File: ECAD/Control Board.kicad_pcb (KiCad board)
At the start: 2 copper layers, 266.1 x 97.2 mm, 77 parts, among them J3 Thermocouple, J4 SD_Card, J5 PWR/Heat, J6 FAN, J7 UPDI, Q1 IPD50N06S4L08, Q2 IPD50N06S4L08, SW1 Reflow, SW2 Stop, SW3 Set temp mode, U1 ATtiny1614-SS, U2 LD1086DT33, U3 AD8497, U4 HT16K33, U5 LM2575HVS-ADJ

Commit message: More routing
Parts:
- moved R5 28.9 mm to (162.8, 77.6)
- moved J7 28.9 mm to (168.9, 75.1)
- moved C12 13.7 mm to (75.8, 104.9)
- moved RV1 13.7 mm to (72.0, 101.1)
- moved R34 5.08 mm to (202.6, 47.0)
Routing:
- net /TempCtrl: track 108.9 -> 7.68 mm
- net /H-: track 0.00 -> 23.1 mm
- net GND: track 82.4 -> 104.7 mm
- net +3V3: track 174.7 -> 156.3 mm
- net Net-(Q1-Pad1): track 5.79 -> 9.46 mm
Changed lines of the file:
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@@
-(kicad_pcb (version 20171130) (host pcbnew "(5.1.9)-1")
+(kicad_pcb (version 20171130) (host pcbnew "(5.1.10)-1")
   (general
     (thickness 1.6)
     (drawings 27)
-    (tracks 444)
+    (tracks 448)
     (zones 0)
     (modules 77)
@@
   )
   (setup
-    (last_trace_width 2.032)
+    (last_trace_width 0.508)
     (user_trace_width 0.254)
     (user_trace_width 0.381)
@@
     (add_net /TOUT)
     (add_net /TempCtrl)
-    (add_net /WRPrt)
     (add_net GND)
     (add_net "Net-(C10-Pad1)")
@@
     (add_net "Net-(D5-Pad2)")
     (add_net "Net-(D6-Pad1)")
-    (add_net "Net-(DS1-Pad3)")
-    (add_net "Net-(DS2-Pad3)")
-    (add_net "Net-(DS3-Pad3)")
     (add_net "Net-(J3-Pad1)")
     (add_net "Net-(J3-Pad2)")
-    (add_net "Net-(J4-Pad8)")
-    (add_net "Net-(J4-Pad9)")
     (add_net "Net-(J7-Pad2)")
     (add_net "Net-(Q1-Pad1)")
@@
     (add_net "Net-(R30-Pad1)")
     (add_net "Net-(R31-Pad1)")
-    (add_net "Net-(U3-Pad4)")
-    (add_net "Net-(U4-Pad10)")
-    (add_net "Net-(U4-Pad11)")
-    (add_net "Net-(U4-Pad8)")
-    (add_net "Net-(U4-Pad9)")
     (add_net VCC)
   )
@@
   )
   (module Resistor_SMD:R_1206_3216Metric_Pad1.30x1.75mm_HandSolder (layer F.Cu)
-    (at 197.485 46.99 270)
+    (at 202.565 46.99 270)
     (descr "Resistor SMD 1206 (3216 Metric), square (rectangular) end terminal, IPC_7351 nominal with elongated pad for handsoldering. (Body size source: IPC-SM-782 page 72, https://www.pcb-3d.com/wordpress/wp-content/uploads/ipc-sm-782a_amendment_1_and_2.pdf), generated with kicad-footprint-generator")
     (tags "resistor handsolder")
@@
   )
   (module Connector_PinHeader_2.54mm:PinHeader_1x03_P2.54mm_Vertical (layer B.Cu)
-    (at 60.325 93.98 180)
+    (at 72.009 101.092 180)
     (descr "Through hole straight pin header, 1x03, 2.54mm pitch, single row")
     (tags "Through hole pin header THT 1x03 2.54mm single row")
@@
   )
   (module Resistor_SMD:R_1206_3216Metric_Pad1.30x1.75mm_HandSolder (layer F.Cu)
-    (at 167.92 106.045)
+    (at 162.84 77.597)
     (descr "Resistor SMD 1206 (3216 Metric), square (rectangular) end terminal, IPC_7351 nominal with elongated pad for handsoldering. (Body size source: IPC-SM-782 page 72, https://www.pcb-3d.com/wordpress/wp-content/uploads/ipc-sm-782a_amendment_1_and_2.pdf), generated with kicad-footprint-generator")
     (tags "resistor handsolder")
@@
   )
   (module Connector_PinHeader_2.54mm:PinHeader_1x03_P2.54mm_Vertical (layer B.Cu)
-    (at 173.99 103.505 180)
+    (at 168.91 75.057 180)
     (descr "Through hole straight pin header, 1x03, 2.54mm pitch, single row")
     (tags "Through hole pin header THT 1x03 2.54mm single row")
@@
   )
   (module Capacitor_SMD:C_0805_2012Metric_Pad1.18x1.45mm_HandSolder (layer F.Cu)
-    (at 64.135 97.79 270)
+    (at 75.819 104.902 270)
     (descr "Capacitor SMD 0805 (2012 Metric), square (rectangular) end terminal, IPC_7351 nominal with elongated pad for handsoldering. (Body size source: IPC-SM-782 page 76, https://www.pcb-3d.com/wordpress/wp-content/uploads/ipc-sm-782a_amendment_1_and_2.pdf, https://docs.google.com/spreadsheets/d/1BsfQQcO9C6DZCsRaXUlFlo91Tg2WpOkGARC1WS5S8t0/edit?usp=sharing), generated with kicad-footprint-generator")
     (tags "capacitor handsolder")
@@
     (effects (font (size 1 1) (thickness 0.15)) (justify mirror))
   )
-  (gr_text UPDI (at 173.99 111.125) (layer B.SilkS)
+  (gr_text UPDI (at 168.91 82.677) (layer B.SilkS)
     (effects (font (size 1 1) (thickness 0.15)) (justify mirror))
   )
@@
   (segment (start 61.305188 73.4275) (end 59.957688 72.08) (width 0.381) (layer F.Cu) (net 1))
   (segment (start 69.469 73.4275) (end 61.305188 73.4275) (width 0.381) (layer F.Cu) (net 1))
-  (segment (start 63.9025 99.06) (end 64.135 98.8275) (width 0.508) (layer F.Cu) (net 1))
-  (segment (start 60.325 99.06) (end 63.9025 99.06) (width 0.508) (layer F.Cu) (net 1))
+  (segment (start 75.5865 106.172) (end 75.819 105.9395) (width 0.508) (layer F.Cu) (net 1))
+  (segment (start 72.009 106.172) (end 75.5865 106.172) (width 0.508) (layer F.Cu) (net 1))
   (via (at 132.715 75.565) (size 1) (drill 0.5) (layers F.Cu B.Cu) (net 1))
   (via (at 146.05 59.055) (size 1) (drill 0.5) (layers F.Cu B.Cu) (net 1))
@@
   (via (at 120.65 92.71) (size 1) (drill 0.5) (layers F.Cu B.Cu) (net 1))
   (via (at 83.82 97.155) (size 1) (drill 0.5) (layers F.Cu B.Cu) (net 1))
-  (via (at 66.04 99.06) (size 1) (drill 0.5) (layers F.Cu B.Cu) (net 1))
+  (via (at 77.724 106.172) (size 1) (drill 0.5) (layers F.Cu B.Cu) (net 1))
   (via (at 61.214 56.515) (size 1) (drill 0.5) (layers F.Cu B.Cu) (net 1))
   (via (at 68.199 75.692) (size 1) (drill 0.5) (layers F.Cu B.Cu) (net 1))
@@
   (segment (start 218.05 101.6) (end 217.805 101.355) (width 2.032) (layer F.Cu) (net 1))
   (segment (start 227.965 101.6) (end 218.05 101.6) (width 2.032) (layer F.Cu) (net 1))
+  (via (at 212.725 95.25) (size 1) (drill 0.5) (layers F.Cu B.Cu) (net 1))
+  (segment (start 222.57 55.88) (end 232.41 65.72) (width 2.54) (layer F.Cu) (net 1))
+  (segment (start 214.19 55.88) (end 222.57 55.88) (width 2.54) (layer F.Cu) (net 1))
   (segment (start 66.8515 71.43) (end 66.929 71.3525) (width 0.381) (layer F.Cu) (net 2))
   (segment (start 63.3265 71.43) (end 66.8515 71.43) (width 0.381) (layer F.Cu) (net 2))
@@
   (segment (start 71.0985 71.3525) (end 69.469 71.3525) (width 0.508) (layer F.Cu) (net 2))
   (segment (start 83.184994 93.98) (end 84.328 92.836994) (width 0.508) (layer B.Cu) (net 2))
-  (segment (start 60.325 93.98) (end 83.184994 93.98) (width 0.508) (layer B.Cu) (net 2))
+  (segment (start 192.945 62.77) (end 193.04 62.865) (width 1.27) (layer F.Cu) (net 2))
+  (segment (start 192.945 58.42) (end 192.945 62.77) (width 1.27) (layer F.Cu) (net 2))
   (segment (start 232.41 84.78) (end 232.41 75.25) (width 2.54) (layer F.Cu) (net 3))
   (segment (start 208.175 92.955) (end 207.87 92.65) (width 1.27) (layer F.Cu) (net 3))
   (segment (start 217.805 92.955) (end 208.175 92.955) (width 1.27) (layer F.Cu) (net 3))
+  (segment (start 224.235 92.955) (end 232.41 84.78) (width 2.032) (layer F.Cu) (net 3))
+  (segment (start 217.805 92.955) (end 224.235 92.955) (width 2.032) (layer F.Cu) (net 3))
+  (segment (start 217.805 92.955) (end 217.805 87.63) (width 2.032) (layer F.Cu) (net 3))
   (segment (start 201.93 58.42) (end 194.945 58.42) (width 0.762) (layer F.Cu) (net 4))
   (segment (start 202.19 58.16) (end 201.93 58.42) (width 1.27) (layer F.Cu) (net 4))
@@
   (segment (start 63.754 64.06) (end 63.754 67.31) (width 0.381) (layer F.Cu) (net 6))
   (segment (start 62.019 67.31) (end 63.754 67.31) (width 0.381) (layer F.Cu) (net 6))
-  (segment (start 63.9025 96.52) (end 64.135 96.7525) (width 0.508) (layer F.Cu) (net 7))
-  (segment (start 60.325 96.52) (end 63.9025 96.52) (width 0.508) (layer F.Cu) (net 7))
-  (segment (start 65.589558 96.7525) (end 64.135 96.7525) (width 0.381) (layer F.Cu) (net 7))
-  (segment (start 71.199058 102.362) (end 65.589558 96.7525) (width 0.381) (layer F.Cu) (net 7))
-  (segment (start 163.068 102.362) (end 71.199058 102.362) (width 0.381) (layer F.Cu) (net 7))
+  (segment (start 75.5865 103.632) (end 75.819 103.8645) (width 0.508) (layer F.Cu) (net 7))
+  (segment (start 72.009 103.632) (end 75.5865 103.632) (width 0.508) (layer F.Cu) (net 7))
   (segment (start 165.735 99.695) (end 163.068 102.362) (width 0.381) (layer F.Cu) (net 7))
   (segment (start 176.175 77.995) (end 175.65 77.47) (width 0.508) (layer F.Cu) (net 8))
@@
   (segment (start 63.754 53.721) (end 66.675 50.8) (width 0.381) (layer F.Cu) (net 31))
   (segment (start 63.754 58.42) (end 63.754 53.721) (width 0.381) (layer F.Cu) (net 31))
-  (via (at 212.725 95.25) (size 1) (drill 0.5) (layers F.Cu B.Cu) (net 1))
-  (segment (start 224.235 92.955) (end 232.41 84.78) (width 2.032) (layer F.Cu) (net 3))
-  (segment (start 217.805 92.955) (end 224.235 92.955) (width 2.032) (layer F.Cu) (net 3))
-  (segment (start 217.805 92.955) (end 217.805 87.63) (width 2.032) (layer F.Cu) (net 3))
   (segment (start 164.465 92.94) (end 166.02449 91.38051) (width 0.381) (layer F.Cu) (net 33))
   (segment (start 164.465 93.915) (end 164.465 92.94) (width 0.381) (layer F.Cu) (net 33))
-  (segment (start 173.99 106.045) (end 169.47 106.045) (width 0.381) (layer F.Cu) (net 37))
+  (segment (start 168.91 77.597) (end 164.39 77.597) (width 0.381) (layer F.Cu) (net 37))
   (segment (start 111.125 94.371888) (end 111.125 95.52) (width 0.381) (layer F.Cu) (net 38))
   (segment (start 106.68 89.926888) (end 111.125 94.371888) (width 0.381) (layer F.Cu) (net 38))
@@
   (segment (start 202.47 42.17) (end 207.89 42.17) (width 0.508) (layer F.Cu) (net 41))
   (segment (start 202.21 41.91) (end 202.47 42.17) (width 0.508) (layer F.Cu) (net 41))
+  (segment (start 202.565 42.265) (end 202.21 41.91) (width 0.508) (layer F.Cu) (net 41))
+  (segment (start 202.565 45.44) (end 202.565 42.265) (width 0.508) (layer F.Cu) (net 41))
   (segment (start 109.22 89.926888) (end 110.378112 91.085) (width 0.381) (layer F.Cu) (net 44))
   (segment (start 109.22 88.925493) (end 109.22 89.926888) (width 0.381) (layer F.Cu) (net 44))
@@
   (segment (start 63.69599 72.44949) (end 63.3265 72.08) (width 0.381) (layer F.Cu) (net 60))
   (segment (start 70.29049 72.44949) (end 63.69599 72.44949) (width 0.381) (layer F.Cu) (net 60))
+  (segment (start 220.67 44.45) (end 232.41 56.19) (width 2.54) (layer F.Cu) (net 61))
+  (segment (start 214.19 44.45) (end 220.67 44.45) (width 2.54) (layer F.Cu) (net 61))
   (segment (start 191.025 93.59) (end 191.135 93.7) (width 0.762) (layer F.Cu) (net 62))
   (segment (start 187.065 93.59) (end 191.025 93.59) (width 0.762) (layer F.Cu) (net 62))
@@
     (polygon
       (pts
-        (xy 194.31 107.315) (xy 194.31 65.405) (xy 226.06 65.405) (xy 226.06 107.315)
+        (xy 194.31 107.315) (xy 194.564 64.516) (xy 226.06 64.516) (xy 226.06 107.315)
       )
     )

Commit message: Routed V0.4 Control Board
Finished routing board, removed ununsed models and footprints, re-exported gerbers and .STEP files
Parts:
- J4: moved to B.Cu
- moved C8 115.8 mm to (169.3, 92.1), turned to 180 degrees
- moved J3 115.6 mm to (163.8, 109.2), turned to 0 degrees
- moved R3 113.4 mm to (166.8, 96.9), turned to 270 degrees
- moved C9 106.4 mm to (164.4, 92.1), turned to 180 degrees
- moved U3 104.2 mm to (164.2, 87.6), turned to 180 degrees
- moved R2 103.9 mm to (160.1, 101.0), turned to 180 degrees
- moved R4 103.8 mm to (161.7, 96.9), turned to 270 degrees
- moved RV1 101.1 mm to (172.8, 108.3), turned to 270 degrees
- moved C12 100.8 mm to (176.7, 104.5), turned to 0 degrees
- moved C6 98.1 mm to (164.5, 82.9), turned to 0 degrees
- moved C10 96.5 mm to (159.4, 92.1), turned to 180 degrees
- moved C7 95.3 mm to (164.5, 80.4), turned to 0 degrees
- moved H3 84.5 mm to (243.8, 49.5), turned to 0 degrees
- moved J6 56.0 mm to (128.9, 106.0), turned to 0 degrees
- moved D5 54.9 mm to (134.0, 111.1), turned to 90 degrees
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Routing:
- net +5V: track 40.6 -> 177.6 mm, vias 0 -> 2
- net /TOUT: track 126.3 -> 26.0 mm, vias 0 -> 2
- net /Gate: track 0.00 -> 78.3 mm, vias 0 -> 2
- net /FanPWM: track 0.00 -> 50.1 mm, vias 0 -> 2
- net +3V3: track 156.3 -> 197.8 mm, vias 2 -> 1
- net /SS: track 0.00 -> 28.6 mm, vias 0 -> 1
- net GND: track 104.7 -> 79.5 mm, vias 27 -> 41
- net /MISO: track 3.18 -> 26.7 mm, vias 0 -> 1
- net /MOSI: track 0.00 -> 21.8 mm, vias 0 -> 1
- net /SDDet: track 0.00 -> 20.7 mm, vias 0 -> 1
- net /SCL: track 70.3 -> 90.3 mm
- net /SCK: track 0.00 -> 19.8 mm, vias 0 -> 1
- net /SDA: track 68.1 -> 84.7 mm
- net /TempCtrl: track 7.68 -> 21.7 mm, vias 0 -> 2
- net /RESET: track 0.00 -> 10.5 mm
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- added copper zone on B.Cu, net GND
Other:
- board size 266.1 x 97.2 mm -> 179.1 x 67.9 mm
- board text added: "5V FAN"
- board text added: "PCB Heater Control Board Rev 0.4"
- board text removed: "PCB Heater Control Board Rev 0.3"

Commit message: BOM Export, minor via edits and gerber re-export
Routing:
- net +3V3: track 197.8 -> 198.6 mm

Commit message: start fixing errors in board
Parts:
- moved U2 0.63 mm to (212.7, 61.6)
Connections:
- U2 pad 1: +5V -> GND
- U2 pad 2: GND -> Net-(C4-Pad1)
- U2 pad 3: Net-(C4-Pad1) -> +5V
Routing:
- net GND: track 79.5 -> 73.2 mm
- net Net-(C4-Pad1): track 20.0 -> 14.3 mm
- net +5V: track 177.6 -> 171.9 mm

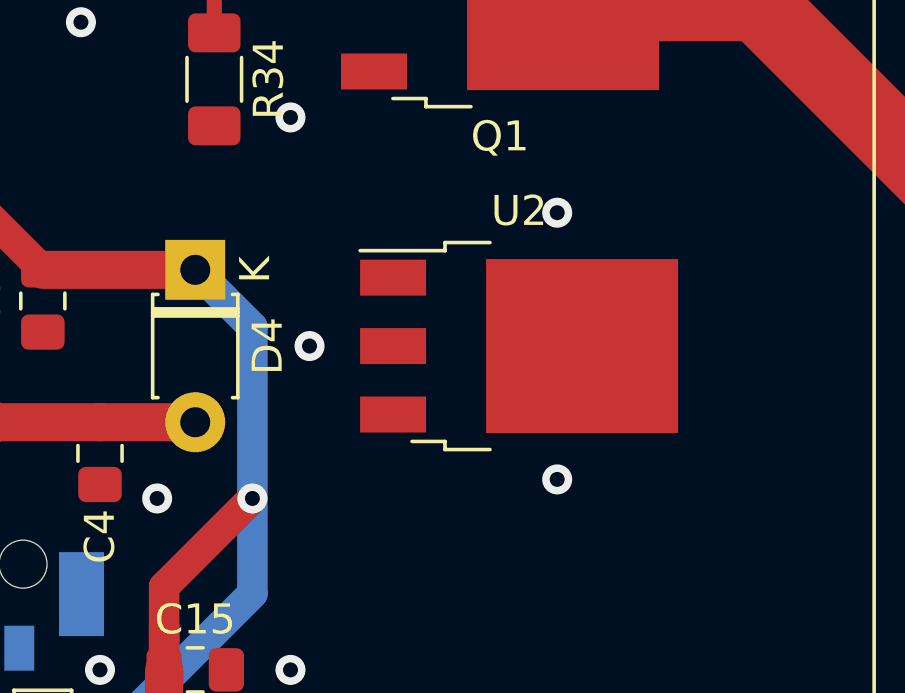
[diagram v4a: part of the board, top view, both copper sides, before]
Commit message: Finish rerouting LDO
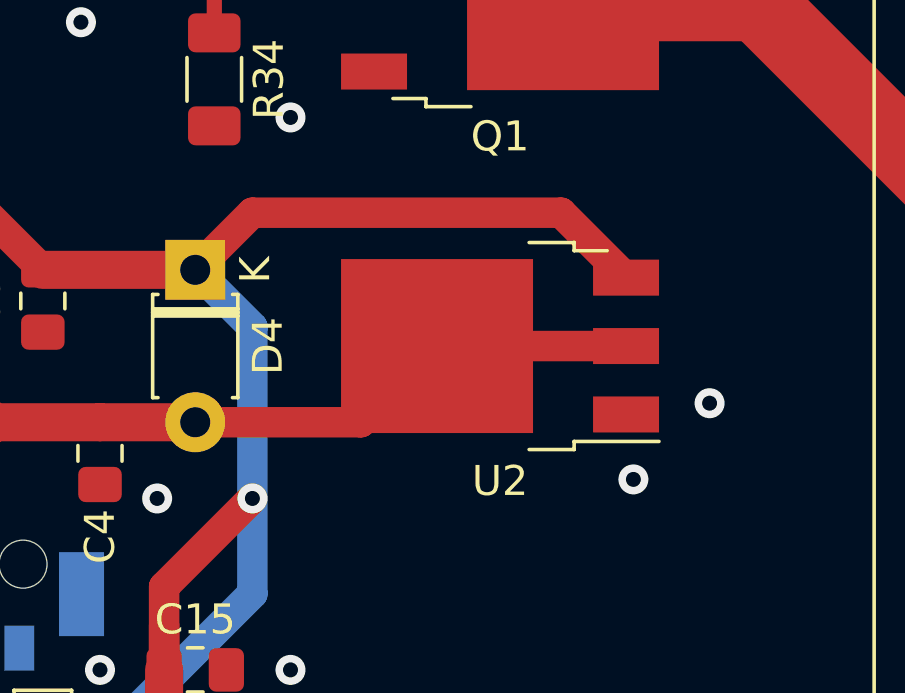
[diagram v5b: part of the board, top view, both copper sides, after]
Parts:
- moved U2 0.63 mm to (212.1, 61.6), turned to 180 degrees
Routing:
- net +5V: track 171.9 -> 188.0 mm
- net Net-(C4-Pad1): track 14.3 -> 29.7 mm
- net GND: vias 41 -> 40

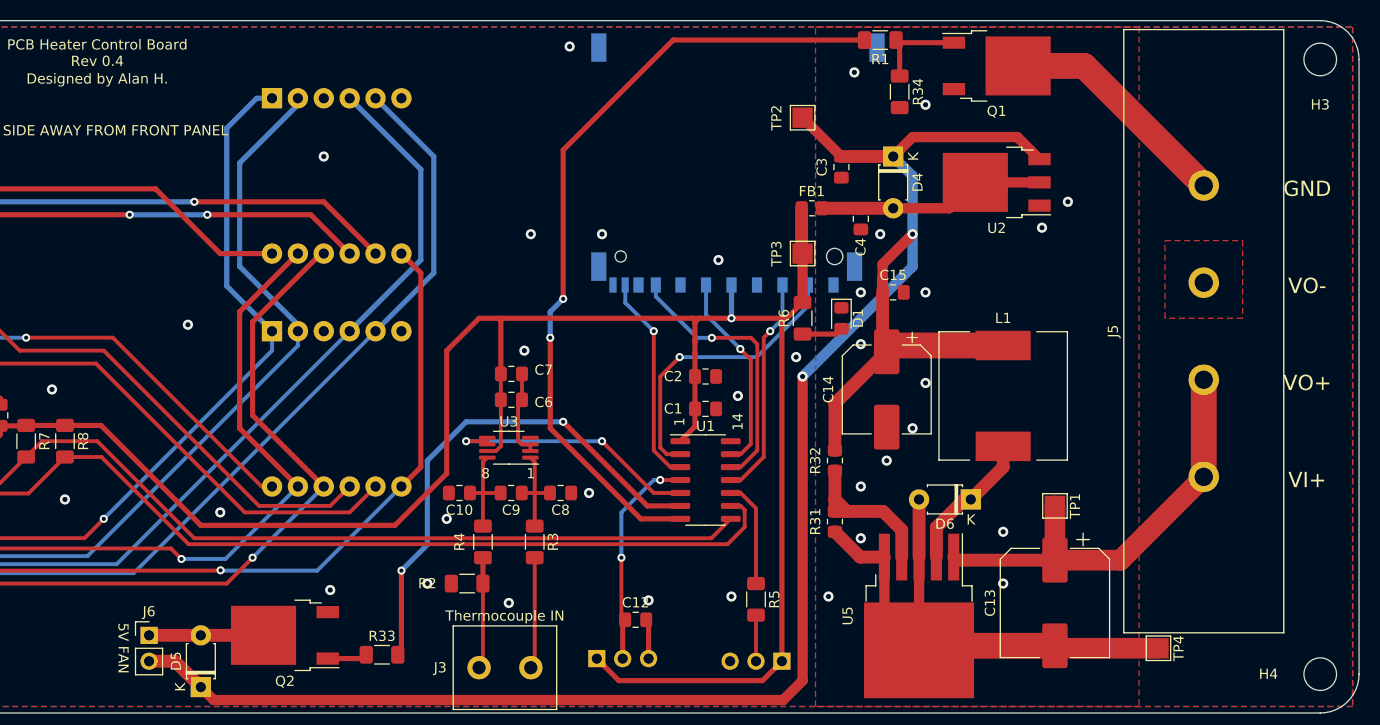
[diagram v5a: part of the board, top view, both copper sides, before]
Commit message: Fix major silkscreen error, push to rev0.5
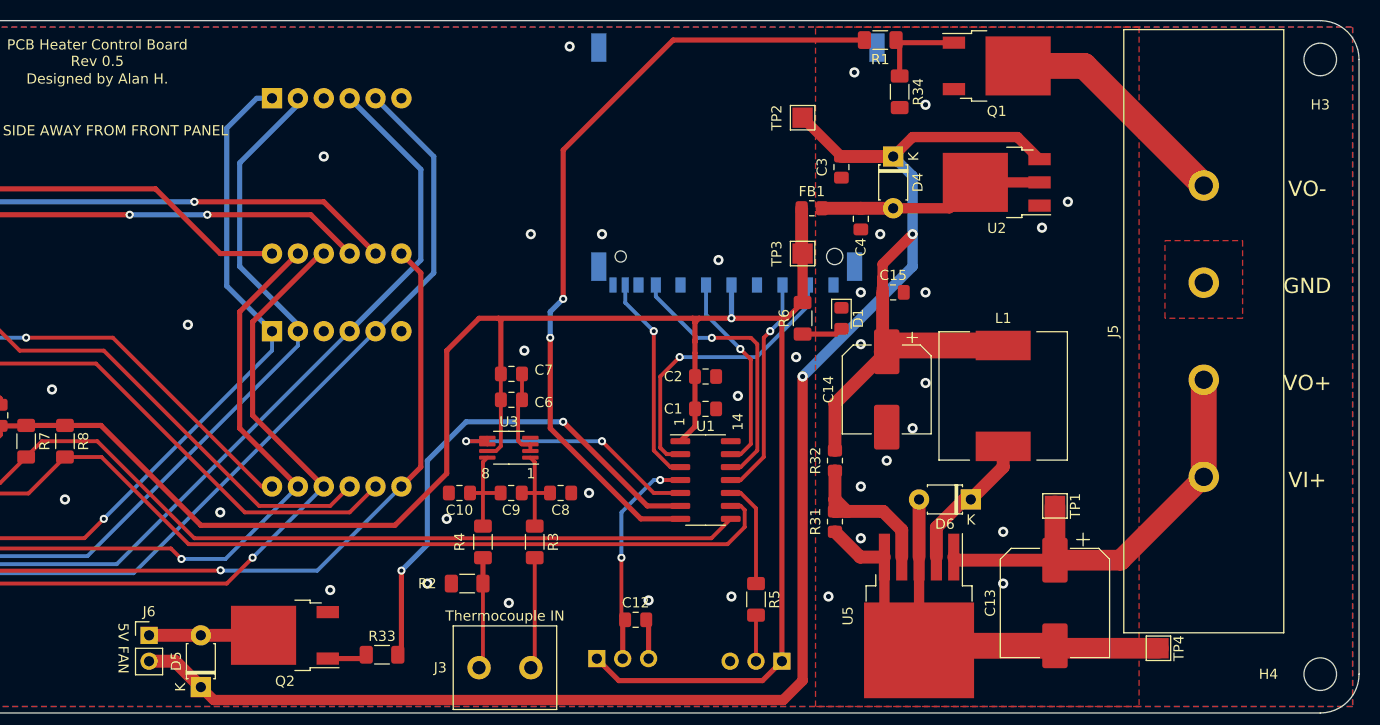
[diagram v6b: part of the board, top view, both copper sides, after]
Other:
- board text added: "PCB Heater Control Board Rev 0.5"
- board text removed: "PCB Heater Control Board Rev 0.4"

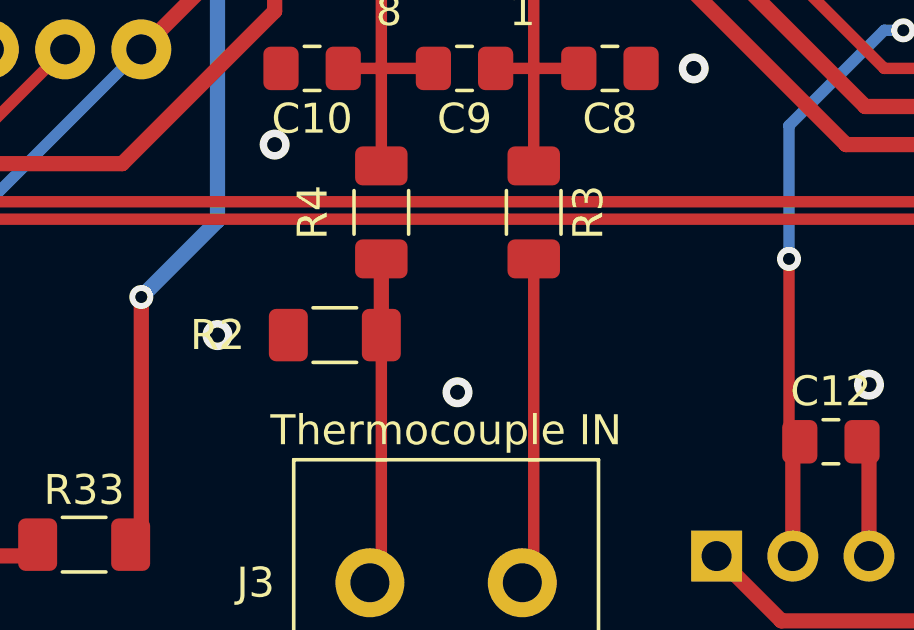
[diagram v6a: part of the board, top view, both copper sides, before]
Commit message: Fix thermocouple + and - pins
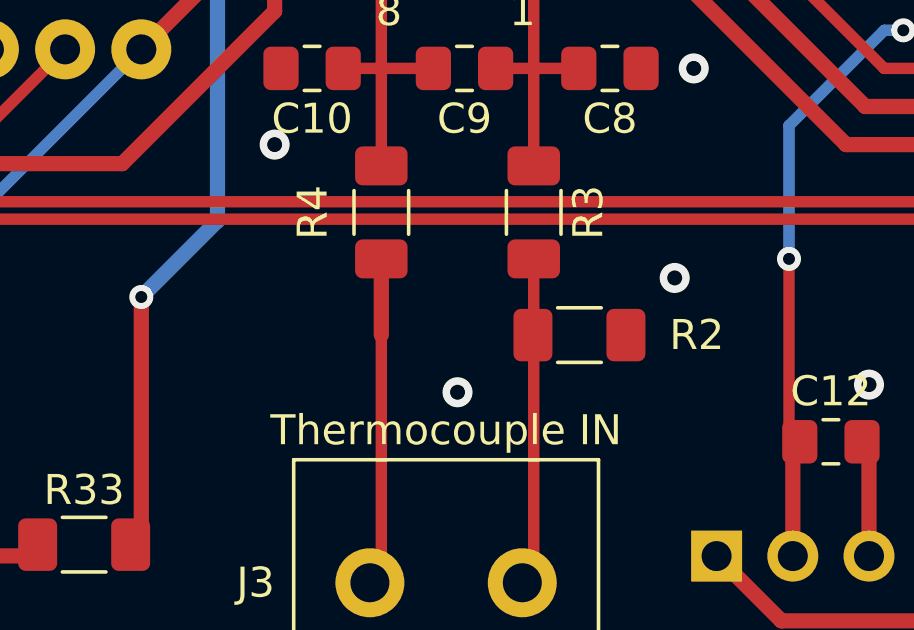
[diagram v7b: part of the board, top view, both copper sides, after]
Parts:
- moved R2 8.15 mm to (168.3, 101.0), turned to 0 degrees
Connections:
- R2 pad 1: Net-(J3-Pad1) -> Net-(J3-Pad2)

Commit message: Push v1.0 release version
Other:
- board text added: "+"
- board text added: "-"
- board text added: "PCB Heater Control Board Rev 1.0"
- board text removed: "PCB Heater Control Board Rev 0.5"
